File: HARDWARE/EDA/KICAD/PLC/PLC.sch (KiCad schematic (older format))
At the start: 164 parts

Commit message: Schematic finished
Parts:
- removed C?: 1000 uF, symbol pspice:C
- added C1: 250V, Capacitor_THT:CP_Radial_D10.0mm_P5.00mm, symbol Device:CP
- added F1, F2: Fuse, Fuse:Fuse_Blade_ATO_directSolder, symbol Device:Fuse
- added J1, J3: retified-output, Connector_Phoenix_MC_HighVoltage:PhoenixContact_MC_1,5_2-G-5.08_1x02_P5.08mm_Horizontal, symbol Connector:Screw_Terminal_01x02
- added J2: power, Connector_Phoenix_MC_HighVoltage:PhoenixContact_MC_1,5_3-G-5.08_1x03_P5.08mm_Horizontal, symbol Connector:Screw_Terminal_01x03
- RV1, RV2, RV3: renamed from RV?; value Varistor -> Varistor 250V; footprint (none) -> Varistor:RV_Disc_D12mm_W4mm_P7.5mm
- gave numbers to parts that had none: 160
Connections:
- net labels added: GNDA
- wire segments 227 -> 242
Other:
- moved on the sheet: D1, D10, D100, D101, D102, D103, D104, D105, D106, D107, D108, D109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

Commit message: pause work
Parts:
- renumbered D157 to D1, D73 to D10, D56 to D100, D68 to D101, D80 to D102, D92 to D103, D116 to D105, D128 to D106, D140 to D107, D152 to D108, D9 to D109, D85 to D11, D21 to D110, D33 to D111, D45 to D112, D57 to D113, D69 to D114, D81 to D115, D93 to D116, D105 to D117, D117 to D118, D129 to D119, D97 to D12, D141 to D120, D153 to D121, D10 to D122, D22 to D123, D34 to D124, D46 to D125, D58 to D126, D70 to D127, D82 to D128, D94 to D129, D109 to D13, D106 to D130, D118 to D131, D130 to D132, D142 to D133, D154 to D134, D11 to D135, D23 to D136, D35 to D137, D47 to D138, D59 to D139, D121 to D14, D71 to D140, D83 to D141, D95 to D142, D107 to D143, D119 to D144, D131 to D145, D143 to D146, D155 to D147, D12 to D148, D24 to D149, D133 to D15, D36 to D150, D48 to D151, D60 to D152, D72 to D153, D84 to D154, D96 to D155, D108 to D156, D120 to D157, D132 to D158, D144 to D159, D145 to D16, D156 to D160, D160 to D17, D2 to D18, D14 to D19, D159 to D2, D26 to D20, D38 to D21, D50 to D22, D62 to D23, D74 to D24, D86 to D25, D98 to D26, D110 to D27, D122 to D28, D134 to D29, D158 to D3, D146 to D30, D3 to D31, D15 to D32, D27 to D33, D39 to D34, D51 to D35, D63 to D36, D75 to D37, D87 to D38, D99 to D39, D1 to D4, D111 to D40, D123 to D41, D135 to D42, D147 to D43, D4 to D44, D16 to D45, D28 to D46, D40 to D47, D52 to D48, D64 to D49, D13 to D5, D76 to D50, D88 to D51, D100 to D52, D112 to D53, D124 to D54, D136 to D55, D148 to D56, D5 to D57, D17 to D58, D29 to D59, D25 to D6, D41 to D60, D53 to D61, D65 to D62, D77 to D63, D89 to D64, D101 to D65, D113 to D66, D125 to D67, D137 to D68, D149 to D69, D37 to D7, D6 to D70, D18 to D71, D30 to D72, D42 to D73, D54 to D74, D66 to D75, D78 to D76, D90 to D77, D102 to D78, D114 to D79, D49 to D8, D126 to D80, D138 to D81, D150 to D82, D7 to D83, D19 to D84, D31 to D85, D43 to D86, D55 to D87, D67 to D88, D79 to D89, D61 to D9, D91 to D90, D103 to D91, D115 to D92, D127 to D93, D139 to D94, D151 to D95, D8 to D96, D20 to D97, D32 to D98, D44 to D99, J3 to J2, J2 to J3

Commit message: adjusting PCB
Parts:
- C1: footprint Capacitor_THT:CP_Radial_D10.0mm_P5.00mm -> Capacitor_THT:CP_Radial_D18.0mm_P7.50mm
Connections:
- net GNDA: now also J2.1 (Pin_1); no longer J2.2 (Pin_2)
- net at C1.1, D1.1 (K), D2.2 (A): now also J2.2 (Pin_2); no longer J2.1 (Pin_1)
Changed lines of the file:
@@
 F 0 "C1" H 10418 1146 50  0000 L CNN
 F 1 "250V" H 10418 1055 50  0000 L CNN
-F 2 "Capacitor_THT:CP_Radial_D10.0mm_P5.00mm" H 10338 950 50  0001 C CNN
+F 2 "Capacitor_THT:CP_Radial_D18.0mm_P7.50mm" H 10338 950 50  0001 C CNN
 F 3 "~" H 10300 1100 50  0001 C CNN
 	1    10300 1100
@@
 L Connector:Screw_Terminal_01x02 J2
 U 1 1 61AC5FE6
-P 10900 850
-F 0 "J2" H 10980 842 50  0000 L CNN
-F 1 "retified-output" H 10450 950 50  0000 L CNN
-F 2 "Connector_Phoenix_MC_HighVoltage:PhoenixContact_MC_1,5_2-G-5.08_1x02_P5.08mm_Horizontal" H 10900 850 50  0001 C CNN
-F 3 "~" H 10900 850 50  0001 C CNN
-	1    10900 850
-	1    0    0    -1
+P 10900 950
+F 0 "J2" H 10980 942 50  0000 L CNN
+F 1 "retified-output" H 10450 750 50  0000 L CNN
+F 2 "Connector_Phoenix_MC_HighVoltage:PhoenixContact_MC_1,5_2-G-5.08_1x02_P5.08mm_Horizontal" H 10900 950 50  0001 C CNN
+F 3 "~" H 10900 950 50  0001 C CNN
+	1    10900 950
+	1    0    0    1
 $EndComp
 $Comp

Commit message: finished project
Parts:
- removed J1: retified-output, Connector_Phoenix_MC_HighVoltage:PhoenixContact_MC_1,5_2-G-5.08_1x02_P5.08mm_Horizontal, symbol Connector:Screw_Terminal_01x02
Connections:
- net GND: now also D109.1 (K); no longer D70.1 (K)
- net GROUP1: now also D56.2 (A); no longer D95.2 (A)
- net at D134.2 (A): now also D70.1 (K); no longer D109.1 (K)
- net at D31.1 (K): now also D95.2 (A); no longer D56.2 (A)
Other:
- moved on the sheet: D100, D101, D102, D103, D104, D105, D106, D107, D108, D109, D110, D111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

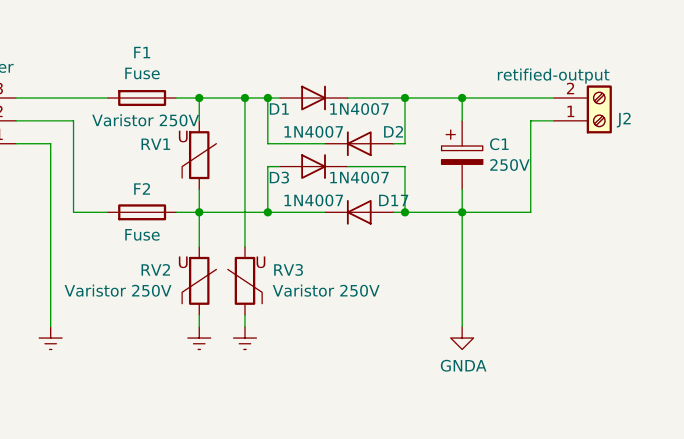
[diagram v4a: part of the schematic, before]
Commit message: Adjust schematic and PCB
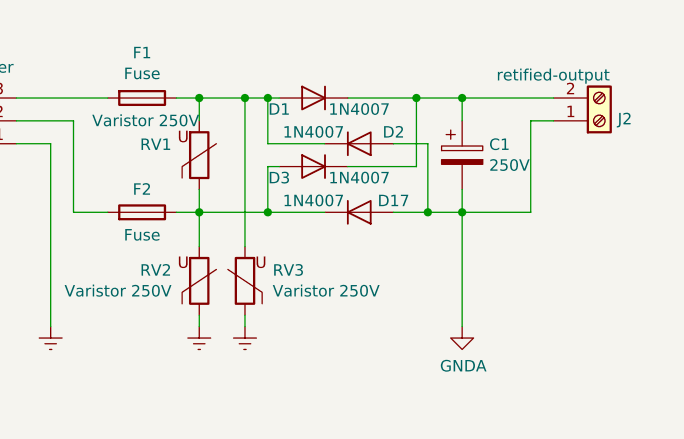
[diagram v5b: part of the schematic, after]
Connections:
- net GNDA: now also D2.2 (A); no longer D3.1 (K)
- net at C1.1, D1.1 (K), J2.2 (Pin_2): now also D3.1 (K); no longer D2.2 (A)

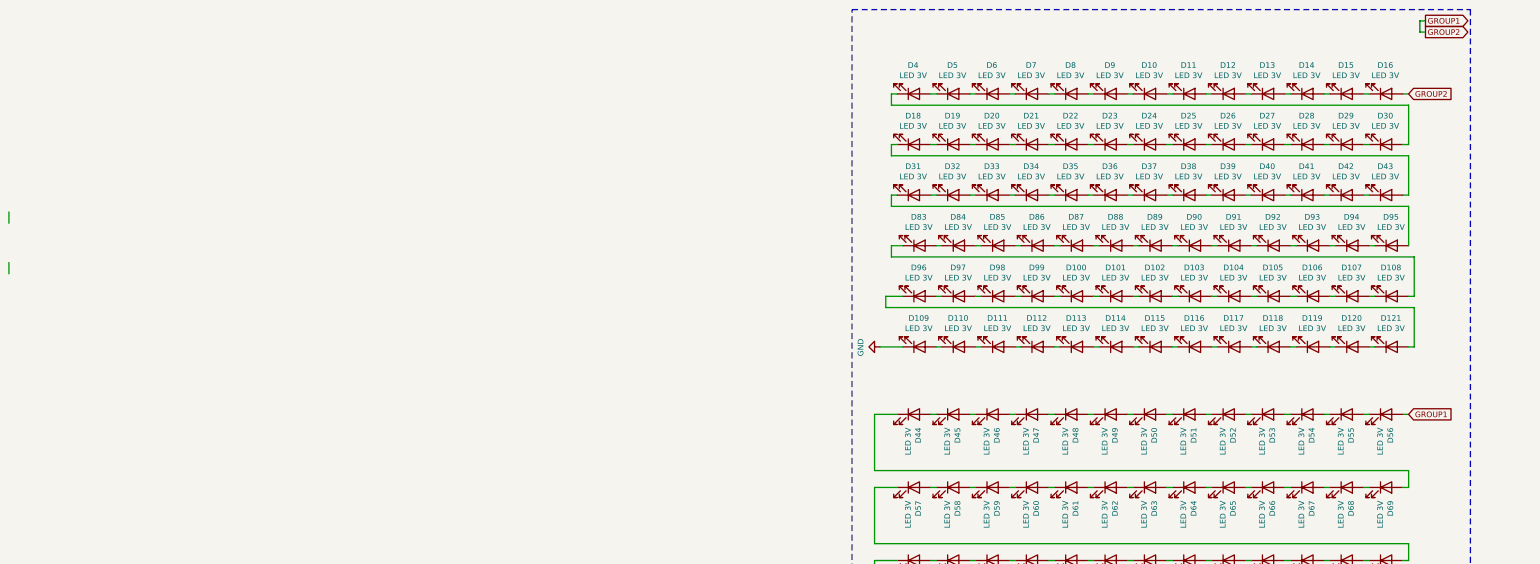
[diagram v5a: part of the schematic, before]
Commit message: adjust schematic group 2
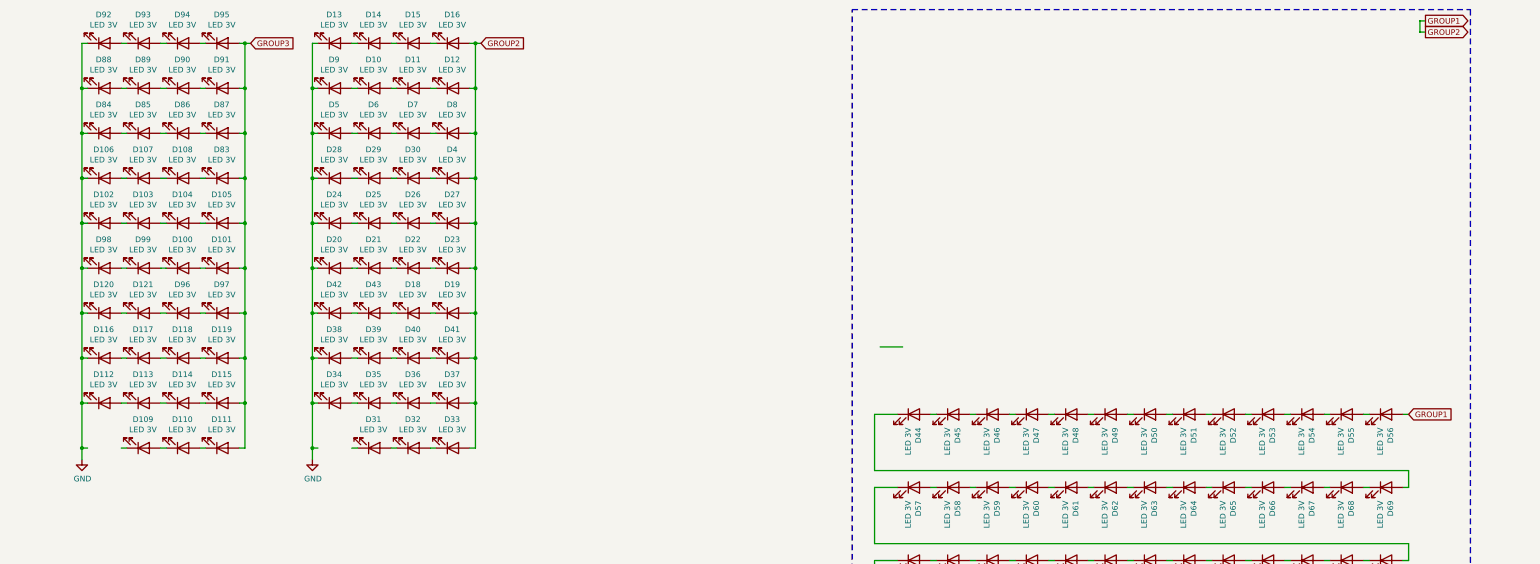
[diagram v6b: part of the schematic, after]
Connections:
- net GND: now also D102.1 (K), D106.1 (K), D112.1 (K), D116.1 (K), D120.1 (K), D13.1 (K), D20.1 (K), D24.1 (K), D28.1 (K), D34.1 (K), D38.1 (K), D42.1 (K), D5.1 (K), D84.1 (K), D88.1 (K), D9.1 (K), D92.1 (K), D98.1 (K); no longer D109.1 (K)
- net GROUP1: now also D12.2 (A), D19.2 (A), D23.2 (A), D27.2 (A), D33.2 (A), D37.2 (A), D4.2 (A), D41.2 (A), D8.2 (A)
- net at D31.1 (K): no longer D95.2 (A)
- net GROUP3: now reaches D91.2 (A)
- net GROUP3: now also D101.2 (A), D105.2 (A), D111.2 (A), D115.2 (A), D119.2 (A), D83.2 (A), D87.2 (A), D95.2 (A), D97.2 (A); no longer D92.1 (K)
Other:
- moved on the sheet: D10, D100, D101, D102, D103, D104, D105, D106, D107, D108, D109, D11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

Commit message: test in pcb
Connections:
- net GROUP3 is gone; now on net GROUP1: D101.2 (A), D105.2 (A), D111.2 (A), D115.2 (A), D119.2 (A), D83.2 (A), D87.2 (A), D91.2 (A), D95.2 (A), D97.2 (A)
- net GND: now also D123.1 (K), D127.1 (K), D131.1 (K), D137.1 (K), D141.1 (K), D145.1 (K), D151.1 (K), D155.1 (K), D159.1 (K), D45.1 (K), D49.1 (K), D53.1 (K), D59.1 (K), D63.1 (K), D67.1 (K), D73.1 (K), D77.1 (K), D81.1 (K); no longer D148.1 (K)
- net GROUP1: now also D122.2 (A), D126.2 (A), D130.2 (A), D134.2 (A), D136.2 (A), D140.2 (A), D144.2 (A), D150.2 (A), D154.2 (A), D158.2 (A), D44.2 (A), D48.2 (A), D52.2 (A), D58.2 (A), D62.2 (A), D66.2 (A), D72.2 (A), D76.2 (A), D80.2 (A)
- net at D70.1 (K): no longer D134.2 (A)
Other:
- moved on the sheet: C1, D1, D10, D100, D101, D102, D103, D104, D105, D106, D107, D108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

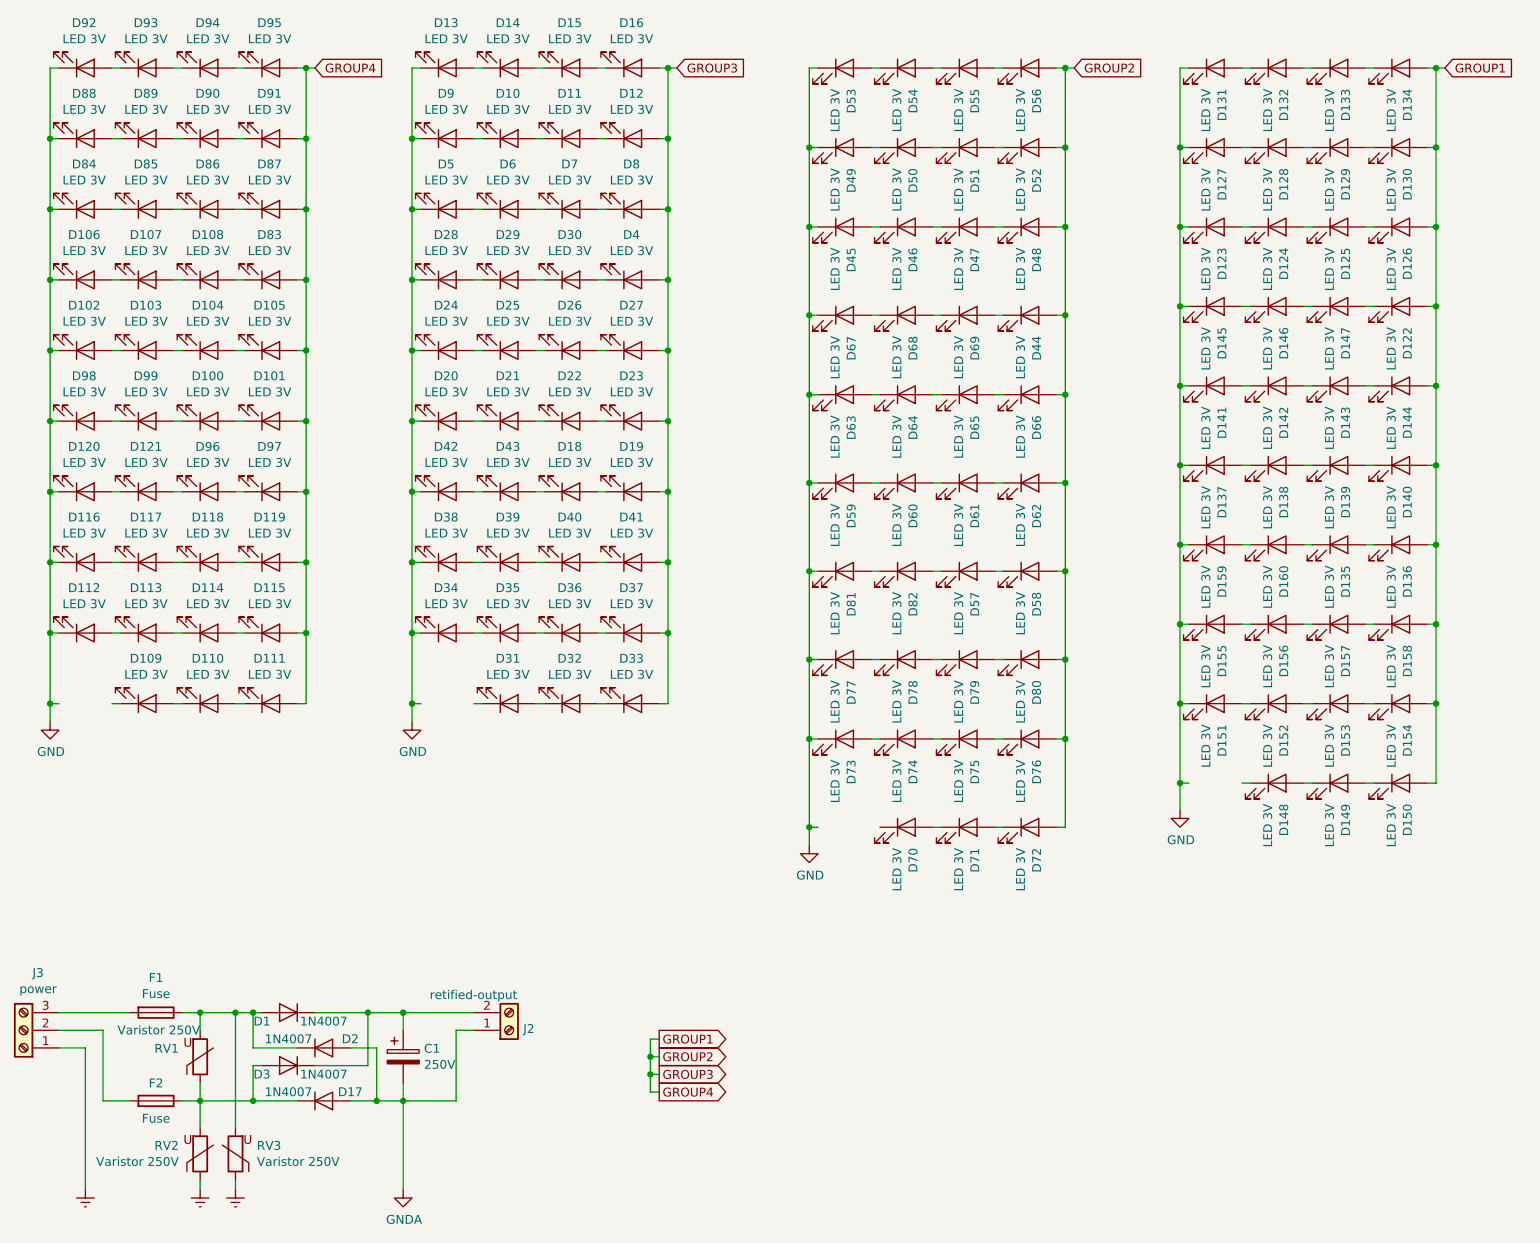
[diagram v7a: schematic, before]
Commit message: reorganized schematic
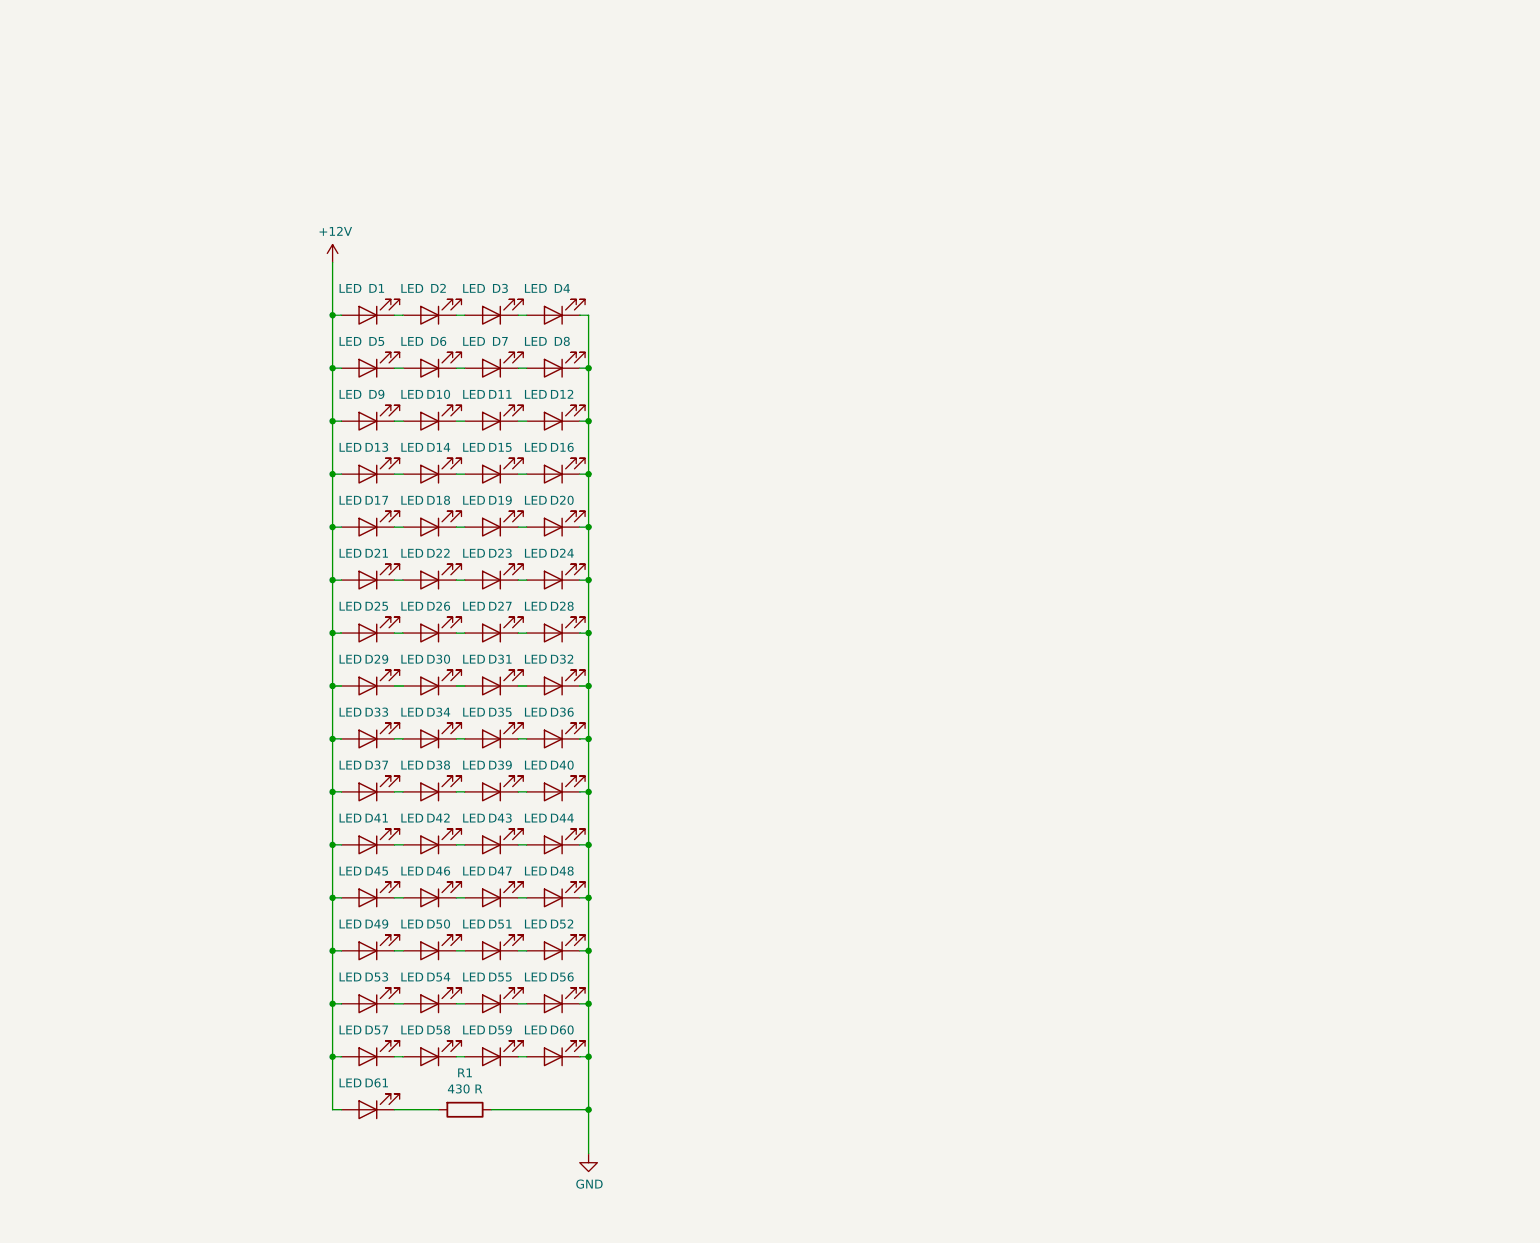
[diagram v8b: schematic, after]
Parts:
- removed C1: 250V, Capacitor_THT:CP_Radial_D18.0mm_P7.50mm, symbol Device:CP
- removed D1, D17, D2, D3: 1N4007, Diode_THT:D_DO-41_SOD81_P10.16mm_Horizontal, symbol Diode:1N4007
- removed D100, D101, D102, D103, D104, D105, D106, D107, D108, D109, D110, D111, D112, D113, D114, D115, D116, D117, D118, D119, D120, D121, D83, D84, D85, D86, D87, D88, D89, D90, D91, D92, D93, D94, D95, D96, D97, D98, D99: LED 3V, LED_THT:LED_D5.0mm_Clear, symbol Device:LED
- removed D122, D123, D124, D125, D126, D127, D128, D129, D130, D131, D132, D133, D134, D135, D136, D137, D138, D139, D140, D141, D142, D143, D144, D145, D146, D147, D148, D149, D150, D151, D152, D153, D154, D155, D156, D157, D158, D159, D160, D62, D63, D64, D65, D66, D67, D68, D69, D70, D71, D72, D73, D74, D75, D76, D77, D78, D79, D80, D81, D82: LED 3V, LED_THT:LED_D5.0mm, symbol Device:LED
- removed F1, F2: Fuse, Fuse:Fuse_Blade_ATO_directSolder, symbol Device:Fuse
- removed J2: retified-output, Connector_Phoenix_MC_HighVoltage:PhoenixContact_MC_1,5_2-G-5.08_1x02_P5.08mm_Horizontal, symbol Connector:Screw_Terminal_01x02
- removed J3: power, Connector_Phoenix_MC_HighVoltage:PhoenixContact_MC_1,5_3-G-5.08_1x03_P5.08mm_Horizontal, symbol Connector:Screw_Terminal_01x03
- removed RV1, RV2, RV3: Varistor 250V, Varistor:RV_Disc_D12mm_W4mm_P7.5mm, symbol Device:Varistor
- added D1, D17, D2, D3: LED, LED_THT:LED_D5.0mm, symbol Device:LED
- added R1: 430 R, Resistor_THT:R_Axial_DIN0207_L6.3mm_D2.5mm_P7.62mm_Horizontal, symbol Device:R
- D10, D11, D12, D25, D26, D27, D28, D41, D42, D43, D9: value LED 3V -> LED; footprint LED_THT:LED_D5.0mm_Clear -> LED_THT:LED_D5.0mm_IRBlack
- D13, D14, D15, D16, D29, D30, D31, D32: value LED 3V -> LED; footprint LED_THT:LED_D5.0mm_Clear -> LED_THT:LED_D5.0mm_IRGrey
- D18, D19, D20, D33, D34, D35, D36, D4: value LED 3V -> LED; footprint LED_THT:LED_D5.0mm_Clear -> LED_THT:LED_D5.0mm
- D21, D22, D23, D24, D37, D38, D39, D40, D49, D5, D50, D51, D52, D6, D7, D8: value LED 3V -> LED
- D44, D57, D58, D59, D60: value LED 3V -> LED; footprint LED_THT:LED_D5.0mm -> LED_THT:LED_D5.0mm_IRBlack
- D45, D46, D47, D48, D61: value LED 3V -> LED; footprint LED_THT:LED_D5.0mm -> LED_THT:LED_D5.0mm_IRGrey
- D53, D54, D55, D56: value LED 3V -> LED; footprint LED_THT:LED_D5.0mm -> LED_THT:LED_D5.0mm_Clear
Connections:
- net GND: now also D12.1 (K), D16.1 (K), D32.1 (K), D36.1 (K), D4.1 (K), D40.1 (K), D44.1 (K), D48.1 (K), D52.1 (K), D56.1 (K), D60.1 (K), D8.1 (K), R1.1; no longer D13.1 (K), D34.1 (K), D38.1 (K), D42.1 (K), D45.1 (K), D49.1 (K), D5.1 (K), D53.1 (K), D59.1 (K), D9.1 (K)
- net at D55.2 (A): now also D54.1 (K); no longer D56.1 (K)
- net at D54.2 (A): now also D53.1 (K); no longer D55.1 (K)
- net +12V: now reaches D53.2 (A)
- net +12V: now also D13.2 (A), D21.2 (A), D25.2 (A), D29.2 (A), D33.2 (A), D37.2 (A), D41.2 (A), D45.2 (A), D49.2 (A), D5.2 (A), D57.2 (A), D61.2 (A), D9.2 (A), D1.2 (A), D17.2 (A); no longer D54.1 (K)
- net at D51.2 (A): now also D50.1 (K); no longer D52.1 (K)
- net at D50.2 (A): now also D49.1 (K); no longer D51.1 (K)
- net at D47.2 (A): now also D46.1 (K); no longer D48.1 (K)
- net at D46.2 (A): now also D45.1 (K); no longer D47.1 (K)
- net at D60.2 (A): now also D59.1 (K); no longer D61.1 (K)
- net at D59.2 (A): now also D58.1 (K); no longer D60.1 (K)
- net at D57.1 (K): now also D58.2 (A)
- net at D15.2 (A): now also D14.1 (K); no longer D16.1 (K)
- net at D14.2 (A): now also D13.1 (K); no longer D15.1 (K)
- net at D11.2 (A): now also D10.1 (K); no longer D12.1 (K)
- net at D10.2 (A): now also D9.1 (K); no longer D11.1 (K)
- net at D7.2 (A): now also D6.1 (K); no longer D8.1 (K)
- net at D6.2 (A): now also D5.1 (K); no longer D7.1 (K)
- net at D30.2 (A): now also D29.1 (K); no longer D4.1 (K)
- net at D30.1 (K): now also D31.2 (A); no longer D29.2 (A)
- net at D28.2 (A): now also D27.1 (K); no longer D29.1 (K)
- net at D26.2 (A): now also D25.1 (K); no longer D27.1 (K)
- net at D26.1 (K): now also D27.2 (A); no longer D25.2 (A)
- net at D24.2 (A): now also D23.1 (K); no longer D25.1 (K)
- net at D22.2 (A): now also D21.1 (K); no longer D23.1 (K)
- net at D22.1 (K): now also D23.2 (A); no longer D21.2 (A)
- net at D20.2 (A): now also D19.1 (K); no longer D21.1 (K)
- net at D18.2 (A): now also D17.1 (K); no longer D19.1 (K)
- net at D18.1 (K): now also D19.2 (A); no longer D43.2 (A)
- net at D42.2 (A): now also D41.1 (K); no longer D43.1 (K)
- net at D40.2 (A): now also D39.1 (K); no longer D41.1 (K)
- net at D39.2 (A): now also D38.1 (K); no longer D40.1 (K)
- net at D38.2 (A): now also D37.1 (K); no longer D39.1 (K)
- net at D36.2 (A): now also D35.1 (K); no longer D37.1 (K)
- net at D35.2 (A): now also D34.1 (K); no longer D36.1 (K)
- net at D34.2 (A): now also D33.1 (K); no longer D35.1 (K)
- net at D32.2 (A): now also D31.1 (K); no longer D33.1 (K)
- removed net GROUP1: D12.2 (A), D16.2 (A), D19.2 (A), D23.2 (A), D27.2 (A), D33.2 (A), D37.2 (A), D4.2 (A), D41.2 (A), D44.2 (A), D48.2 (A), D52.2 (A), D56.2 (A), D58.2 (A), D8.2 (A)
- new net: D1.1 (K), D2.2 (A)
- new net: D2.1 (K), D3.2 (A)
- new net: D3.1 (K), D4.2 (A)
- new net: D7.1 (K), D8.2 (A)
- new net: D11.1 (K), D12.2 (A)
- new net: D15.1 (K), D16.2 (A)
- new net: D42.1 (K), D43.2 (A)
- new net: D43.1 (K), D44.2 (A)
- new net: D47.1 (K), D48.2 (A)
- new net: D51.1 (K), D52.2 (A)
- new net: D55.1 (K), D56.2 (A)
- new net: D61.1 (K), R1.2
